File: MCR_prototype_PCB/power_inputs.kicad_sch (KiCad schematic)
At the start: 11 parts, among them J1 Conn_01x20_Pin, U20 LM2596T-5, U21 LM2596T-3.3

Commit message: Add files via upload
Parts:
- C5, C7: footprint (none) -> Capacitor_THT:CP_Radial_D10.0mm_P5.00mm; KiLib_Generator (none) -> capacitor/THT/other
- C6, C8: footprint (none) -> Capacitor_THT:CP_Radial_D8.0mm_P3.50mm; KiLib_Generator (none) -> capacitor/THT/other
- D1, D2: KiLib_Generator (none) -> diode/THT
- J1: footprint (none) -> Connector_PinHeader_2.54mm:PinHeader_1x20_P2.54mm_Horizontal; KiLib_Generator (none) -> connector/pin_header_socket
- L1, L2: footprint (none) -> Inductor_SMD:L_Bourns_SRR1260
- U20, U21: KiLib_Generator (none) -> package/TO_SOT/THT
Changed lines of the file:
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@@
+			)
+		)
+		(property "KiLib_Generator" "diode/THT"
+			(at 125.73 77.47 0)
+			(hide yes)
+			(show_name no)
+			(do_not_autoplace no)
+			(effects
+				(font
+					(size 1.27 1.27)
+				)
 			)
 		)
@@
 			)
 		)
-		(property "Footprint" ""
+		(property "Footprint" "Inductor_SMD:L_Bourns_SRR1260"
 			(at 132.08 73.66 0)
 			(hide yes)
@@
 			)
 		)
+		(property "KiLib_Generator" "diode/THT"
+			(at 124.46 39.37 0)
+			(hide yes)
+			(show_name no)
+			(do_not_autoplace no)
+			(effects
+				(font
+					(size 1.27 1.27)
+				)
+			)
+		)
 		(pin "1"
 		)
@@
 			)
 		)
-		(property "Footprint" ""
+		(property "Footprint" "Capacitor_THT:CP_Radial_D10.0mm_P5.00mm"
 			(at 82.55 71.12 0)
 			(hide yes)
@@
 		)
 		(property "Description" "capacitor, small US symbol"
+			(at 82.55 71.12 0)
+			(hide yes)
+			(show_name no)
+			(do_not_autoplace no)
+			(effects
+				(font
+					(size 1.27 1.27)
+				)
+			)
+		)
+		(property "KiLib_Generator" "capacitor/THT/other"
 			(at 82.55 71.12 0)
 			(hide yes)
@@
 			)
 		)
-		(property "Footprint" ""
+		(property "Footprint" "Inductor_SMD:L_Bourns_SRR1260"
 			(at 130.81 35.56 0)
 			(hide yes)
@@
 			)
 		)
+		(property "KiLib_Generator" "package/TO_SOT/THT"
+			(at 104.14 33.02 0)
+			(hide yes)
+			(show_name no)
+			(do_not_autoplace no)
+			(effects
+				(font
+					(size 1.27 1.27)
+				)
+			)
+		)
 		(pin "5"
 		)
@@
 			)
 		)
-		(property "Footprint" ""
+		(property "Footprint" "Capacitor_THT:CP_Radial_D10.0mm_P5.00mm"
 			(at 82.55 33.02 0)
 			(hide yes)
@@
 		)
 		(property "Description" "capacitor, small US symbol"
+			(at 82.55 33.02 0)
+			(hide yes)
+			(show_name no)
+			(do_not_autoplace no)
+			(effects
+				(font
+					(size 1.27 1.27)
+				)
+			)
+		)
+		(property "KiLib_Generator" "capacitor/THT/other"
 			(at 82.55 33.02 0)
 			(hide yes)
@@
 			)
 		)
+		(property "KiLib_Generator" "package/TO_SOT/THT"
+			(at 104.14 71.12 0)
+			(hide yes)
+			(show_name no)
+			(do_not_autoplace no)
+			(effects
+				(font
+					(size 1.27 1.27)
+				)
+			)
+		)
 		(pin "1"
 		)
@@
 			)
 		)
-		(property "Footprint" ""
+		(property "Footprint" "Connector_PinHeader_2.54mm:PinHeader_1x20_P2.54mm_Horizontal"
 			(at 34.29 50.8 0)
 			(hide yes)
@@
 		)
 		(property "Description" "Generic connector, single row, 01x20, script generated"
+			(at 34.29 50.8 0)
+			(hide yes)
+			(show_name no)
+			(do_not_autoplace no)
+			(effects
+				(font
+					(size 1.27 1.27)
+				)
+			)
+		)
+		(property "KiLib_Generator" "connector/pin_header_socket"
 			(at 34.29 50.8 0)
 			(hide yes)
@@
 			)
 		)
-		(property "Footprint" ""
+		(property "Footprint" "Capacitor_THT:CP_Radial_D8.0mm_P3.50mm"
 			(at 137.16 38.1 0)
 			(hide yes)
@@
 		)
 		(property "Description" "capacitor, small US symbol"
+			(at 137.16 38.1 0)
+			(hide yes)
+			(show_name no)
+			(do_not_autoplace no)
+			(effects
+				(font
+					(size 1.27 1.27)
+				)
+			)
+		)
+		(property "KiLib_Generator" "capacitor/THT/other"
 			(at 137.16 38.1 0)
 			(hide yes)
@@
 			)
 		)
-		(property "Footprint" ""
+		(property "Footprint" "Capacitor_THT:CP_Radial_D8.0mm_P3.50mm"
 			(at 138.43 76.2 0)
 			(hide yes)
@@
 			(at 138.43 76.2 0)
 			(hide yes)
+			(show_name no)
+			(do_not_autoplace no)
+			(effects
+				(font
+					(size 1.27 1.27)
+				)
+			)
+		)
+		(property "KiLib_Generator" "capacitor/THT/other"
+			(at 138.43 76.2 0)
+			(hide yes)

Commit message: Updated 8/22/26
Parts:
- removed C6, C8: 220 uF, Capacitor_THT:CP_Radial_D8.0mm_P3.50mm, symbol Device:C_Small_US
- removed D1, D2: 1N5824, Diode_THT:D_DO-201AD_P15.24mm_Horizontal, symbol Diode:1N5822
- removed U20: LM2596T-5, Package_TO_SOT_THT:TO-220-5_P3.4x3.7mm_StaggerOdd_Lead3.8mm_Vertical, symbol Regulator_Switching:LM2596T-5
- removed U21: LM2596T-3.3, Package_TO_SOT_THT:TO-220-5_P3.4x3.7mm_StaggerOdd_Lead3.8mm_Vertical, symbol Regulator_Switching:LM2596T-3.3
- added D1, D2, D3: LED, LED_SMD:LED_0805_2012Metric_Pad1.15x1.40mm_HandSolder, symbol Device:LED
- added R6: 2k ohm, Resistor_SMD:R_0805_2012Metric_Pad1.20x1.40mm_HandSolder, symbol Device:R_Small_US
- added R7: 510 ohm, Resistor_SMD:R_0805_2012Metric_Pad1.20x1.40mm_HandSolder, symbol Device:R_Small_US
- added R8: 220 ohm, Resistor_SMD:R_0805_2012Metric_Pad1.20x1.40mm_HandSolder, symbol Device:R_Small_US
- added U24: R-78B5.0-2.0, Converter_DCDC:Converter_DCDC_RECOM_R-78B-2.0_THT, symbol Converter_DCDC:R-78B5.0-2.0
- added U25: R-78B3.3-2.0, Converter_DCDC:Converter_DCDC_RECOM_R-78B-2.0_THT, symbol Converter_DCDC:R-78B3.3-2.0
- C5, C7: value 680 uF -> 4.7 uF 50V
- L1, L2: value 33 uH -> 3.3 uH
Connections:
- net +12V: now also L1.1, L2.1, R6.1
- net +3.3V: now also R8.1, U25.3 (OUT); no longer L2.2
- net +5V: now also R7.1, U24.3 (OUT); no longer L1.2
- net GND: now also D1.1 (K), D2.1 (K), D3.1 (K), U24.2 (GND), U25.2 (GND)
- new net: L2.2, U25.1 (IN)
- new net: D1.2 (A), R6.2
- new net: D2.2 (A), R7.2
- new net: D3.2 (A), R8.2
- new net: L1.2, U24.1 (IN)
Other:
- moved on the sheet: L1, L2

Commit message: Add files via upload
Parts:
- added TP1: +12V Input, TestPoint:TestPoint_Loop_D1.80mm_Drill1.0mm_Beaded, symbol Connector:TestPoint
- added TP2: +3.3V Power, TestPoint:TestPoint_Loop_D1.80mm_Drill1.0mm_Beaded, symbol Connector:TestPoint
- added TP3: +5V Power, TestPoint:TestPoint_Loop_D1.80mm_Drill1.0mm_Beaded, symbol Connector:TestPoint
- added TP4: Gnd, TestPoint:TestPoint_Loop_D1.80mm_Drill1.0mm_Beaded, symbol Connector:TestPoint
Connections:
- net +12V: now also TP1.1
- net +3.3V: now also TP2.1
- net +5V: now also TP3.1
- net GND: now also TP4.1

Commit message: Add files via upload
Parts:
- added C48, C50: 0.1 uF, Capacitor_SMD:C_0805_2012Metric, symbol Device:C_Small_US
- added C49, C51: 100 uF, Capacitor_SMD:CP_Elec_6.3x5.4, symbol Device:C_Small_US
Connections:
- net +3.3V: now also C50.1, C51.1
- net +5V: now also C48.1, C49.1
- net GND: now also C48.2, C49.2, C50.2, C51.2

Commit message: Add files via upload
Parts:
- added C10, C9: 10 uF 50V, Capacitor_THT:CP_Radial_D10.0mm_P5.00mm, symbol Device:C_Small_US
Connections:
- net GND: now also C10.2, C9.2
- net at L2.2, U25.1 (IN): now also C9.1
- net at L1.2, U24.1 (IN): now also C10.1

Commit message: September 8 Version
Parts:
- L1, L2: value 3.3 uH -> FAUL1360-3R3MT; LCSC (none) -> C5298330
- U24: value R-78B5.0-2.0 -> K7805-2000R3; LCSC (none) -> C18212380
- U25: value R-78B3.3-2.0 -> K7803-2000R3; LCSC (none) -> C18212378
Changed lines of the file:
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@@
 			)
 		)
-		(property "Value" "3.3 uH"
+		(property "Value" "FAUL1360-3R3MT"
 			(at 97.79 66.04 90)
 			(show_name no)
@@
 		(property "Description" "Inductor, small symbol"
 			(at 97.79 68.58 0)
+			(hide yes)
+			(show_name no)
+			(do_not_autoplace no)
+			(effects
+				(font
+					(size 1.27 1.27)
+				)
+			)
+		)
+		(property "LCSC" "C5298330"
+			(at 97.79 68.58 90)
 			(hide yes)
 			(show_name no)
@@
 			)
 		)
-		(property "Value" "3.3 uH"
+		(property "Value" "FAUL1360-3R3MT"
 			(at 88.9 27.94 90)
 			(show_name no)
@@
 		(property "Description" "Inductor, small symbol"
 			(at 88.9 30.48 0)
+			(hide yes)
+			(show_name no)
+			(do_not_autoplace no)
+			(effects
+				(font
+					(size 1.27 1.27)
+				)
+			)
+		)
+		(property "LCSC" "C5298330"
+			(at 88.9 30.48 90)
 			(hide yes)
 			(show_name no)
@@
 			)
 		)
-		(property "Value" "R-78B3.3-2.0"
+		(property "Value" "K7803-2000R3"
 			(at 110.49 64.77 0)
 			(show_name no)
@@
 		)
 		(property "Description" "2A Step-Down DC/DC-Regulator, 4.75-32V input, 3.3V fixed Output Voltage, LM78xx replacement, -40°C to +85°C, SIP3"
+			(at 110.49 68.58 0)
+			(hide yes)
+			(show_name no)
+			(do_not_autoplace no)
+			(effects
+				(font
+					(size 1.27 1.27)
+				)
+			)
+		)
+		(property "LCSC" "C18212378"
 			(at 110.49 68.58 0)
 			(hide yes)
@@
 			)
 		)
-		(property "Value" "R-78B5.0-2.0"
+		(property "Value" "K7805-2000R3"
 			(at 104.14 26.67 0)
 			(show_name no)
@@
 			(at 104.14 30.48 0)
 			(hide yes)
+			(show_name no)
+			(do_not_autoplace no)
+			(effects
+				(font
+					(size 1.27 1.27)
+				)
+			)
+		)
+		(property "LCSC" "C18212380 "
+			(at 104.14 30.48 0)
+			(hide yes)

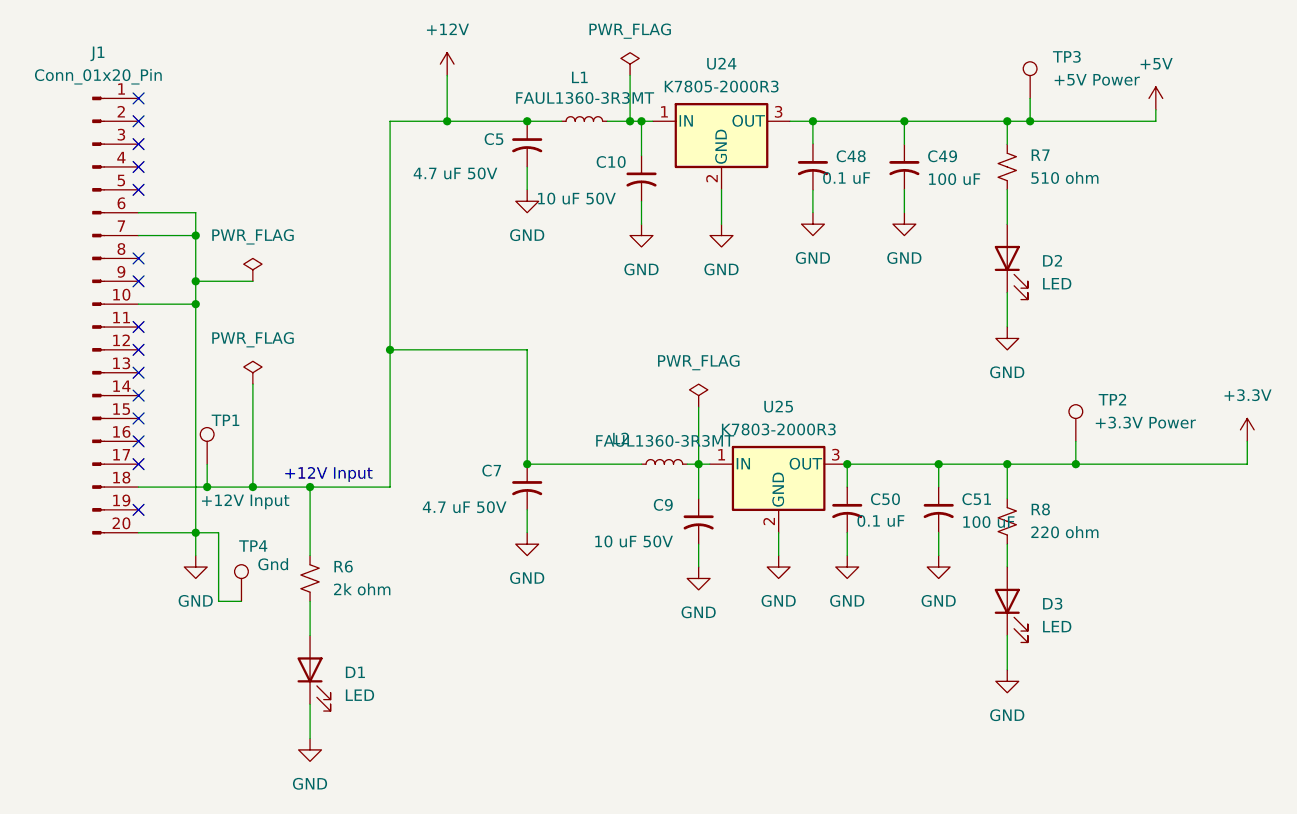
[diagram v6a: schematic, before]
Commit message: Production/schematics for 10/10/26 first board run
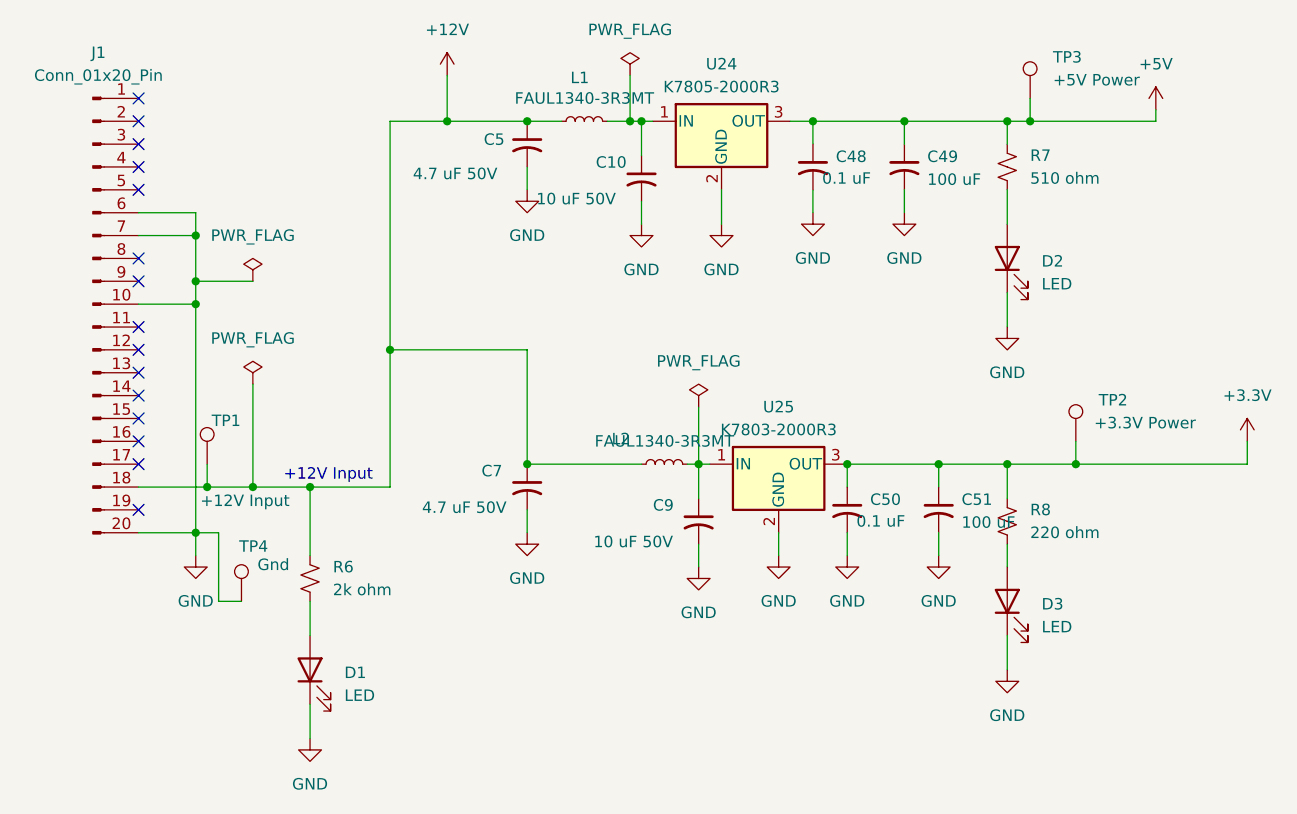
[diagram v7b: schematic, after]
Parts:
- C10, C9: footprint Capacitor_THT:CP_Radial_D10.0mm_P5.00mm -> Capacitor_SMD:CP_Elec_6.3x5.4; LCSC (none) -> C970657
- C48, C50: LCSC (none) -> C49678
- C49, C51: LCSC (none) -> C37308
- C5, C7: footprint Capacitor_THT:CP_Radial_D10.0mm_P5.00mm -> Capacitor_SMD:CP_Elec_4x5.4; LCSC (none) -> C970652
- D1, D2, D3: LCSC (none) -> C84256
- L1, L2: value FAUL1360-3R3MT -> FAUL1340-3R3MT; footprint Inductor_SMD:L_Bourns_SRR1260 -> Inductor_SMD:L_TechFuse_SL1250; LCSC C5298330 -> C5298306
- R6: LCSC (none) -> C17604
- R7: LCSC (none) -> C17734
- R8: LCSC (none) -> C17557
- TP1, TP2, TP3, TP4: footprint TestPoint:TestPoint_Loop_D1.80mm_Drill1.0mm_Beaded -> TestPoint:TestPoint_Pad_1.5x1.5mm
- U24: LCSC C18212380 -> C18212380
